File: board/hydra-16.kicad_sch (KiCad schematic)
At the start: 25 parts, among them J1 Conn_01x32, J2 Conn_01x24, J3 DE9_Plug, U1 74F573, U2 74F541, U3 AT28C64B, U4 W65C02SxP, U5 6522, U6 6551, U7 MAX232, U8 628512_DIP32, U9 74LS154

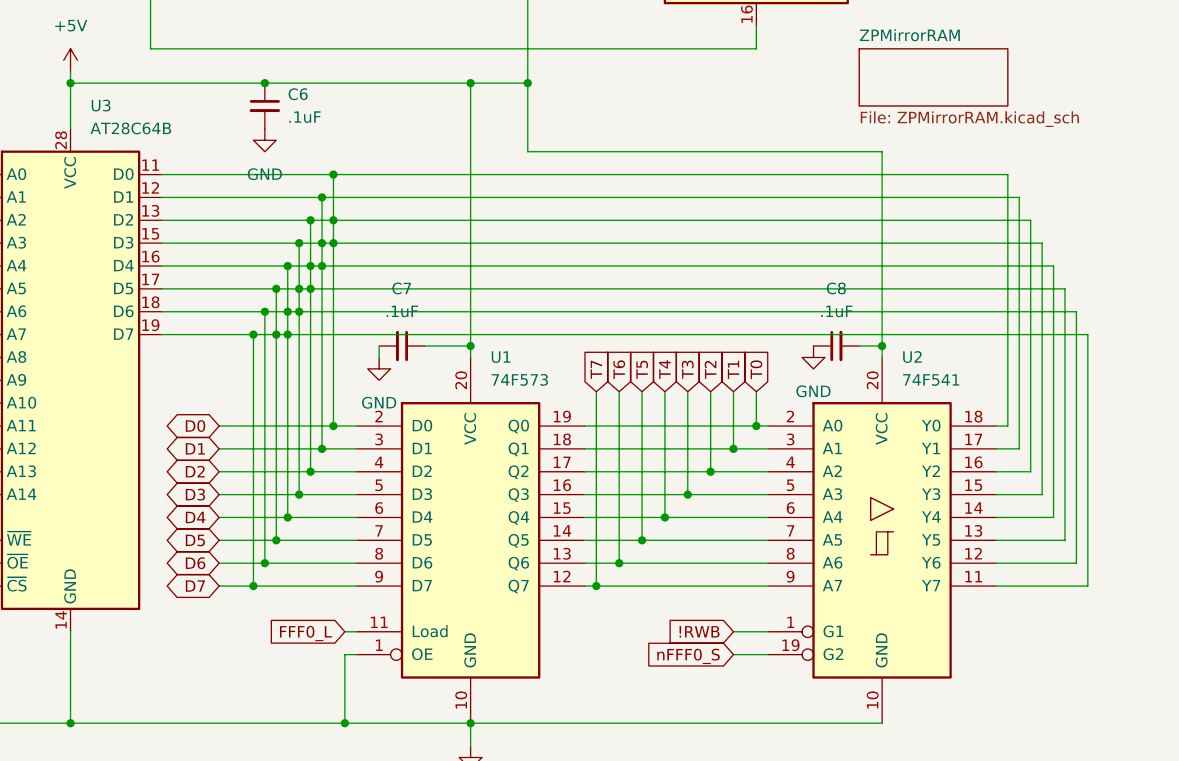
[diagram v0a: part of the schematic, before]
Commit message: Fixing pin assignments
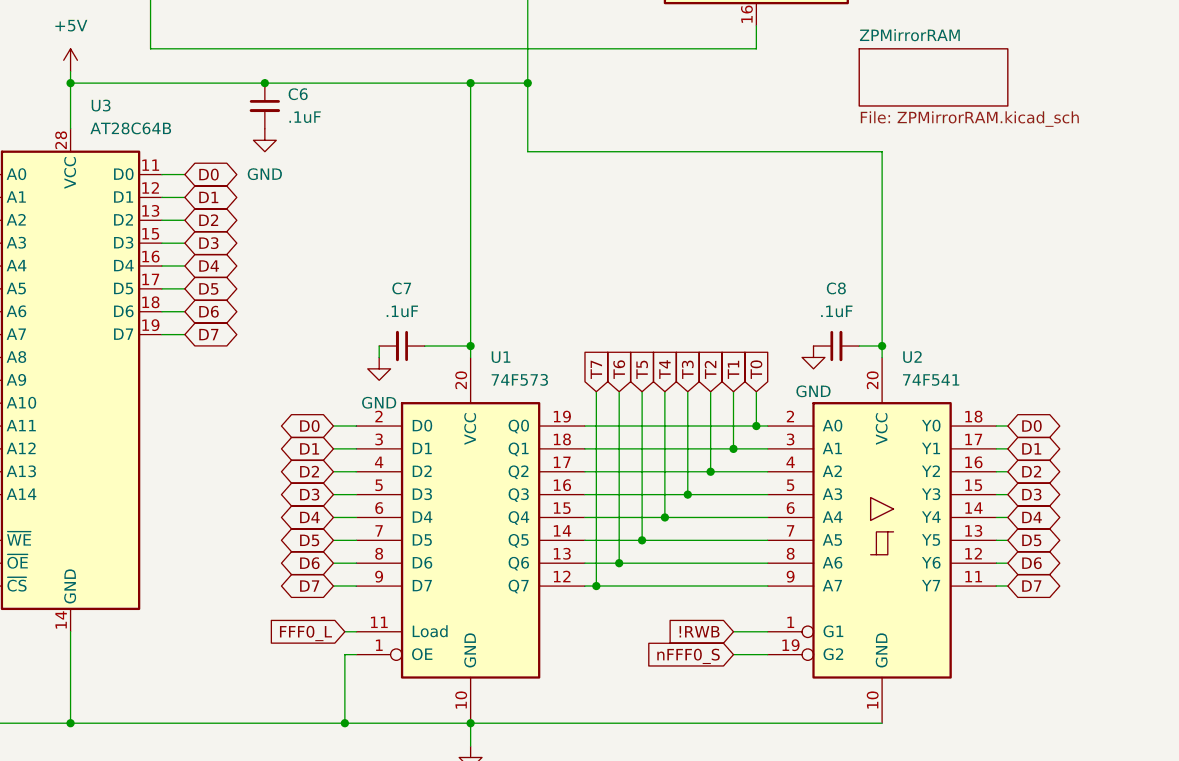
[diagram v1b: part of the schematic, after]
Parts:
- C1, C2, C3, C4, C5: footprint Capacitor_THT:CP_Radial_Tantal_D4.5mm_P2.50mm -> Capacitor_THT:C_Disc_D5.0mm_W2.5mm_P2.50mm
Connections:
- net D0: no longer J2.2 (Pin_2), J2.3 (Pin_3), J2.4 (Pin_4), J2.5 (Pin_5), J2.6 (Pin_6), J2.7 (Pin_7), J2.8 (Pin_8), U1.3 (D1), U1.4 (D2), U1.5 (D3), U1.6 (D4), U1.7 (D5), U1.8 (D6), U1.9 (D7), U2.11 (Y7), U2.12 (Y6), U2.13 (Y5), U2.14 (Y4), U2.15 (Y3), U2.16 (Y2), U2.17 (Y1), U3.12 (D1), U3.13 (D2), U3.15 (D3), U3.16 (D4), U3.17 (D5), U3.18 (D6), U3.19 (D7), U4.26 (D7), U4.27 (D6), U4.28 (D5), U4.29 (D4), U4.30 (D3), U4.31 (D2), U4.32 (D1), U5.26 (D7), U5.27 (D6), U5.28 (D5), U5.29 (D4), U5.30 (D3), U5.31 (D2), U5.32 (D1), U6.19 (D1), U6.20 (D2), U6.21 (D3), U6.22 (D4), U6.23 (D5), U6.24 (D6), U6.25 (D7), U8.14 (Q1), U8.15 (Q2), U8.17 (Q3), U8.18 (Q4), U8.19 (Q5), U8.20 (Q6), U8.21 (Q7)
- new net D1: J2.2 (Pin_2), U1.3 (D1), U2.17 (Y1), U3.12 (D1), U4.32 (D1), U5.32 (D1), U6.19 (D1), U8.14 (Q1)
- new net D2: J2.3 (Pin_3), U1.4 (D2), U2.16 (Y2), U3.13 (D2), U4.31 (D2), U5.31 (D2), U6.20 (D2), U8.15 (Q2)
- new net D3: J2.4 (Pin_4), U1.5 (D3), U2.15 (Y3), U3.15 (D3), U4.30 (D3), U5.30 (D3), U6.21 (D3), U8.17 (Q3)
- new net D4: J2.5 (Pin_5), U1.6 (D4), U2.14 (Y4), U3.16 (D4), U4.29 (D4), U5.29 (D4), U6.22 (D4), U8.18 (Q4)
- new net D5: J2.6 (Pin_6), U1.7 (D5), U2.13 (Y5), U3.17 (D5), U4.28 (D5), U5.28 (D5), U6.23 (D5), U8.19 (Q5)
- new net D6: J2.7 (Pin_7), U1.8 (D6), U2.12 (Y6), U3.18 (D6), U4.27 (D6), U5.27 (D6), U6.24 (D6), U8.20 (Q6)
- new net D7: J2.8 (Pin_8), U1.9 (D7), U2.11 (Y7), U3.19 (D7), U4.26 (D7), U5.26 (D7), U6.25 (D7), U8.21 (Q7)

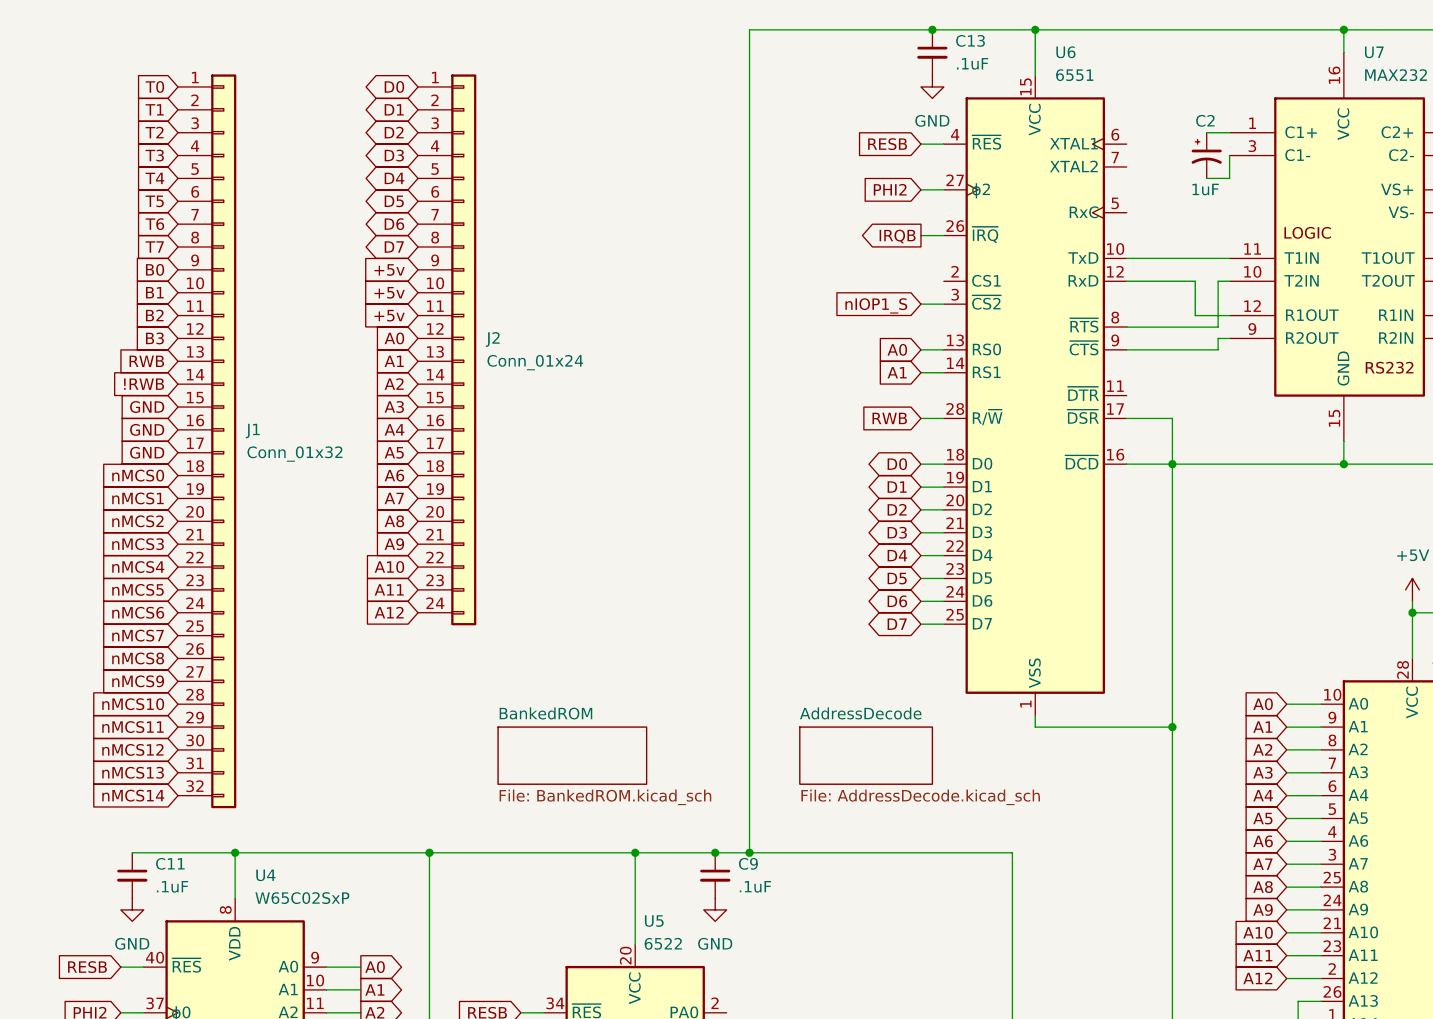
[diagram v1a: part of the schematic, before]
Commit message: Added clocks and power connector.
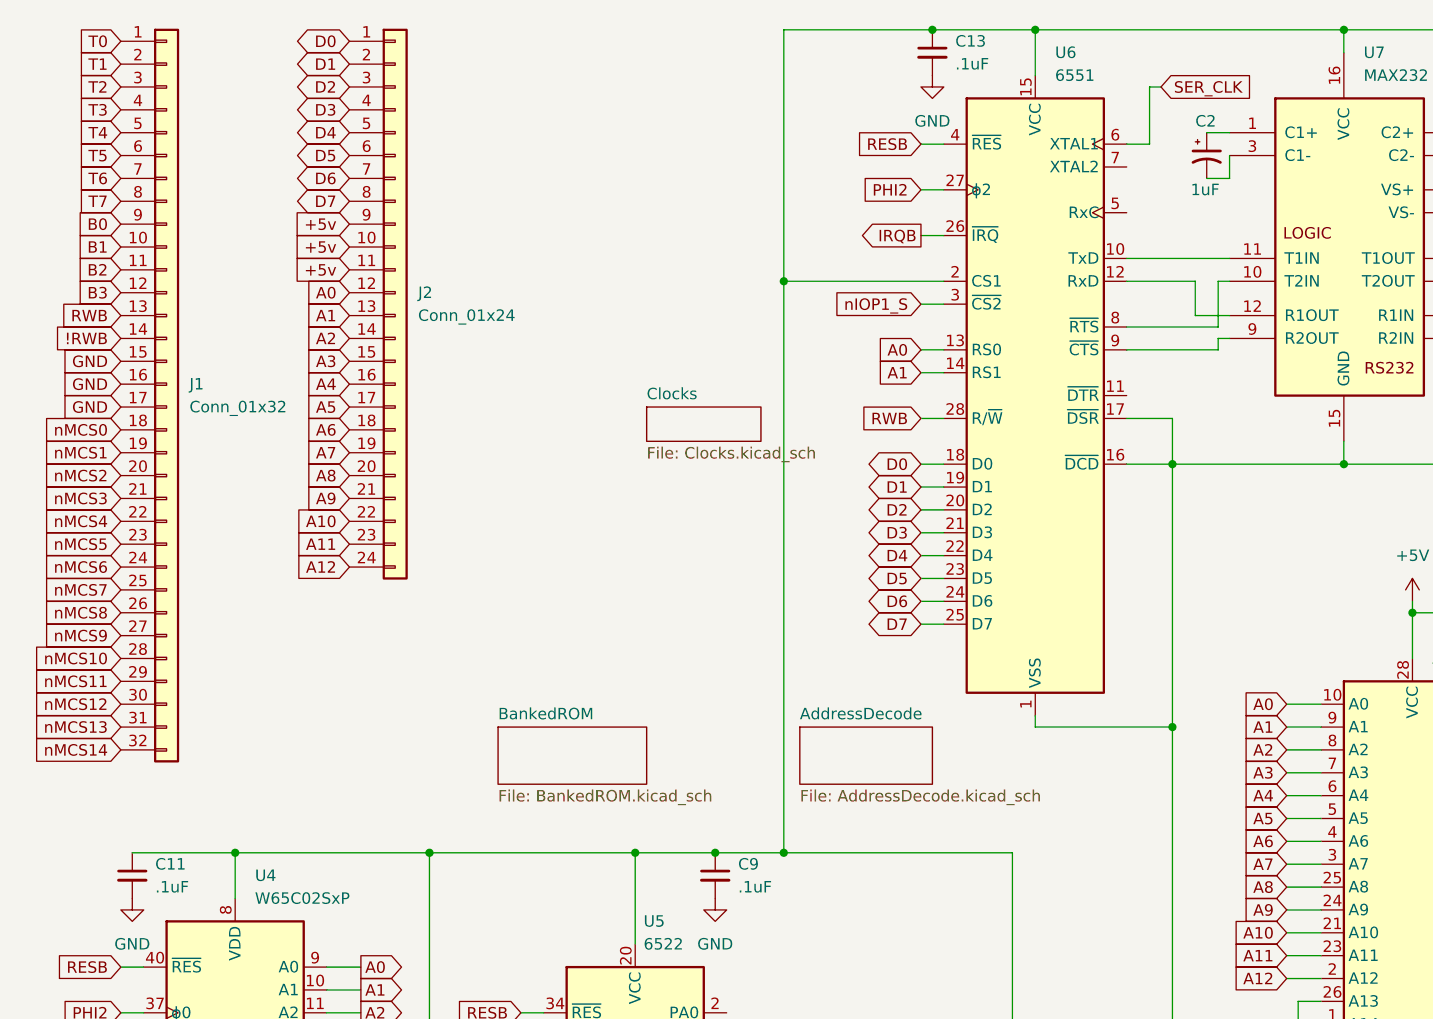
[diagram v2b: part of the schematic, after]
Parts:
- U4, U5: footprint Package_DIP:DIP-40_W15.24mm_LongPads -> Package_DIP:DIP-40_W15.24mm_Socket_LongPads
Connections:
- net +5V: now also U6.2 (CS1)
- net SER_CLK: now reaches U6.6 (XTAL1)
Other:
- added sheet Clocks (Clocks.kicad_sch)
- moved on the sheet: J1, J2

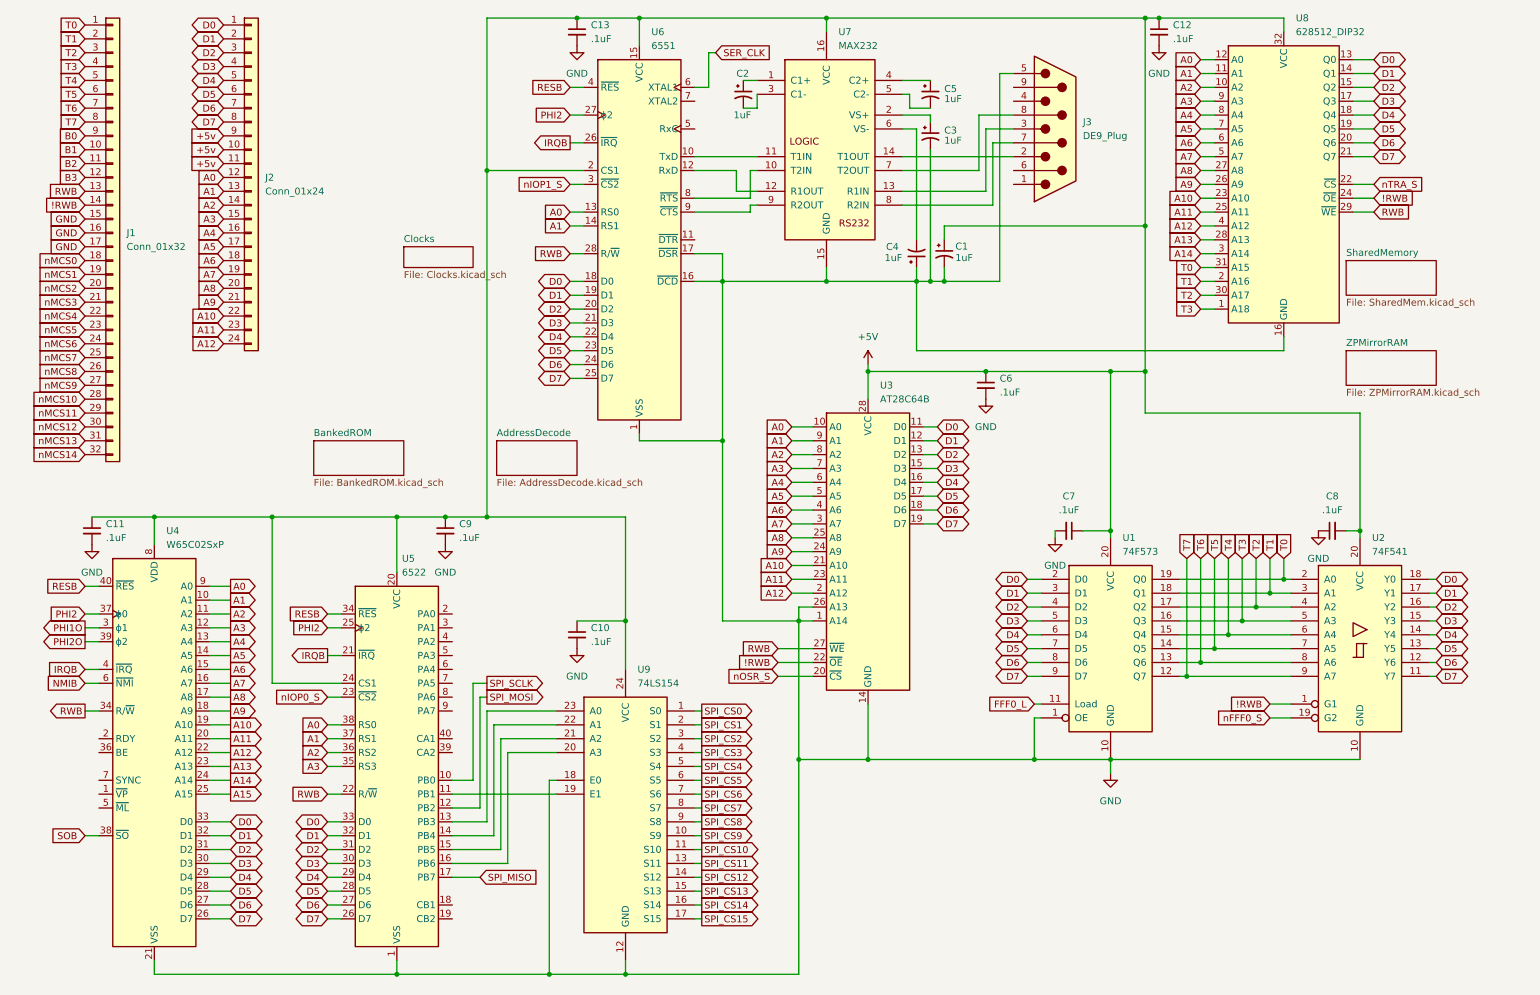
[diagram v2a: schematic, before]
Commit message: More routing changes and board layout optimizations.
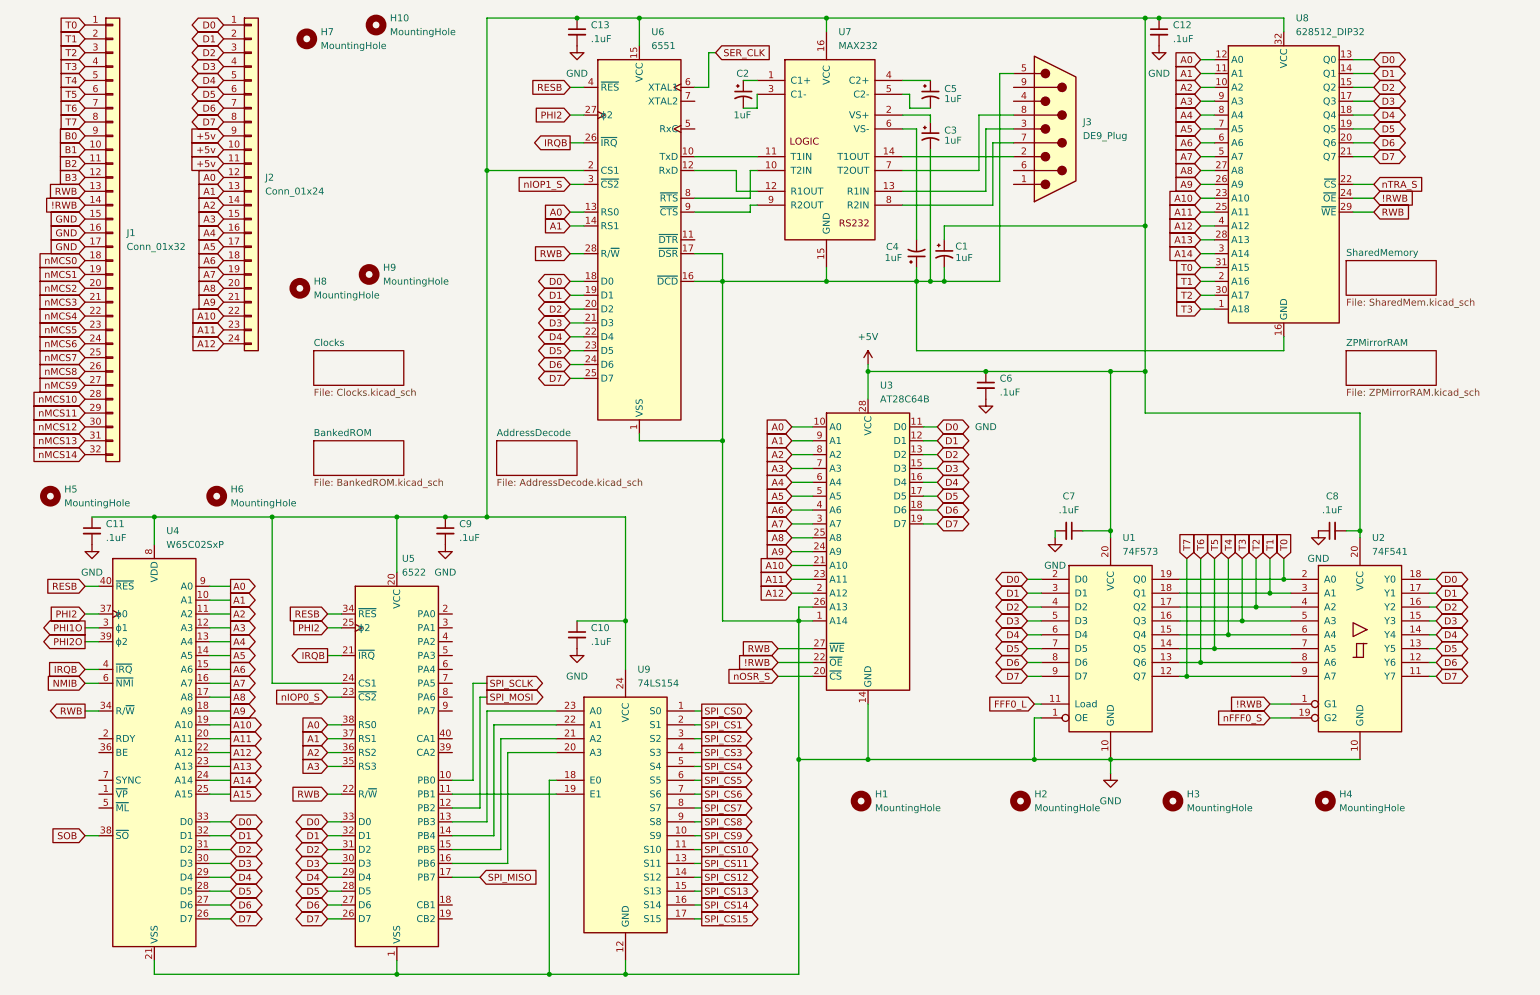
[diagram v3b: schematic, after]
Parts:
- added H1, H10, H2, H3, H4, H5, H6, H7, H8, H9: MountingHole, MountingHole:MountingHole_3.2mm_M3, symbol Mechanical:MountingHole
